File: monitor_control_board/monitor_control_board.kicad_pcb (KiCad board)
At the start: 2 copper layers, 50 x 58 mm, 21 parts, among them J2 Conn_01x08_Male, J3 Conn_01x08_Male, J5 Conn_01x05_Male, J6 Conn_01x05_Male, SW1 SW_Push, SW2 SW_Push, SW3 SW_Push, SW4 SW_Push, SW5 SW_Push, SW6 SW_Push, U1 TSSP58038

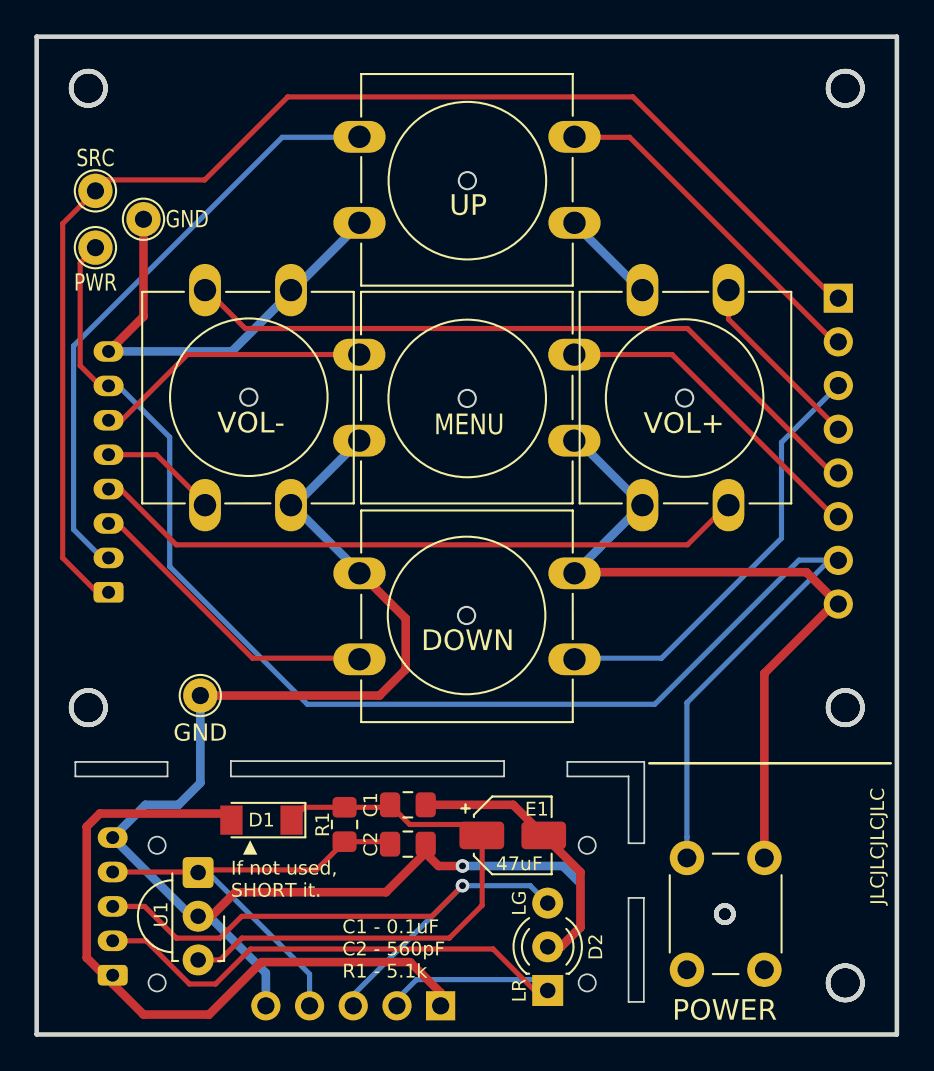
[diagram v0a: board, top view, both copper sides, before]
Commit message: 배선 및 레이아웃 최적화
Signed-off-by: Ju, Gyeong-min <jcmh74@gmail.com>
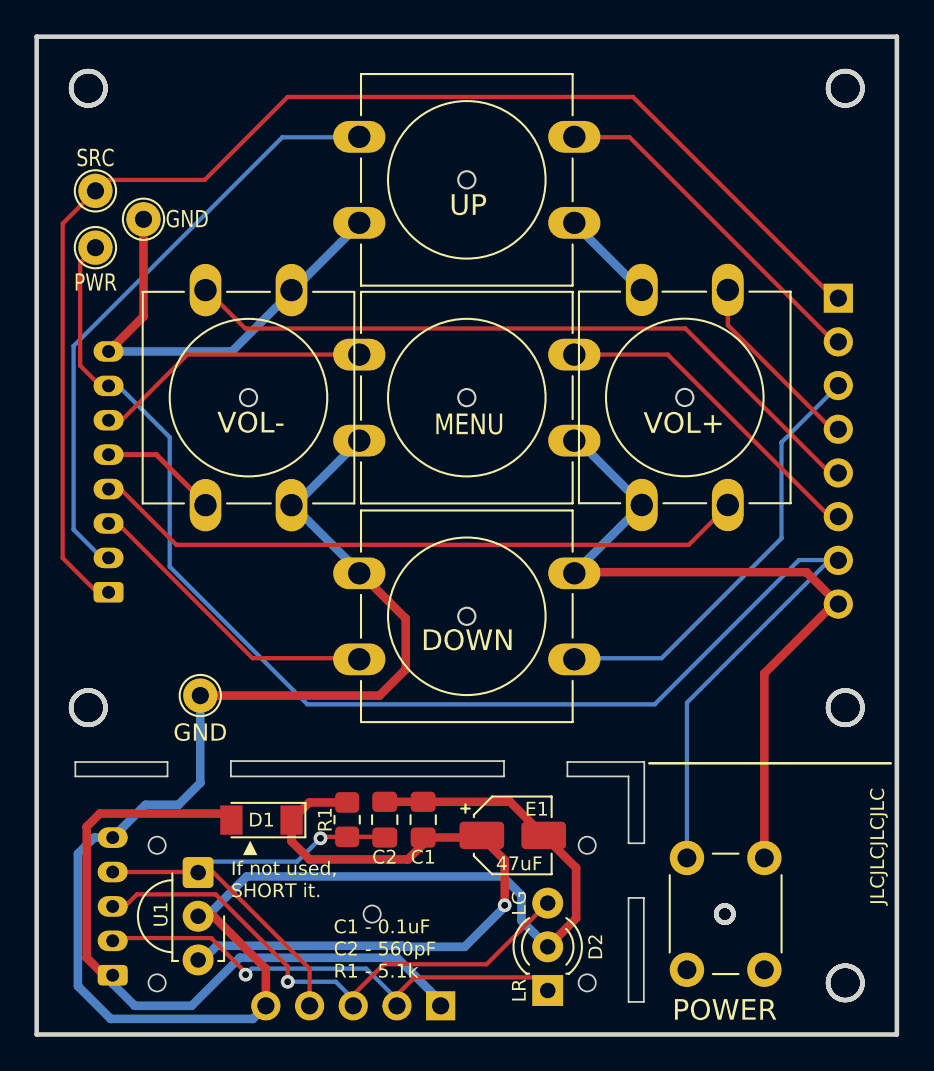
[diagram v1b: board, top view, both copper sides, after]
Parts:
- moved C2 1.96 mm to (148.9, 107.3), turned to 90 degrees
- moved C1 1.24 mm to (151.1, 107.3), turned to 90 degrees
- moved R1 0.32 mm to (146.7, 107.3)
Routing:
- net GND: track 178.4 -> 188.9 mm, vias 1 -> 0
- net /LED_R: track 38.0 -> 28.9 mm, vias 0 -> 1
- net Net-(C1-Pad1): track 34.0 -> 41.0 mm, vias 0 -> 1
- net /LED_G: track 37.3 -> 31.8 mm
- net +5V: track 41.5 -> 41.0 mm
- net /IRIN: vias 0 -> 1
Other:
- outline, holes or cut-outs redrawn

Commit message: osd 컨트롤 보드 GND 핀 추가
Signed-off-by: Ju, Gyeong-min <jcmh74@gmail.com>
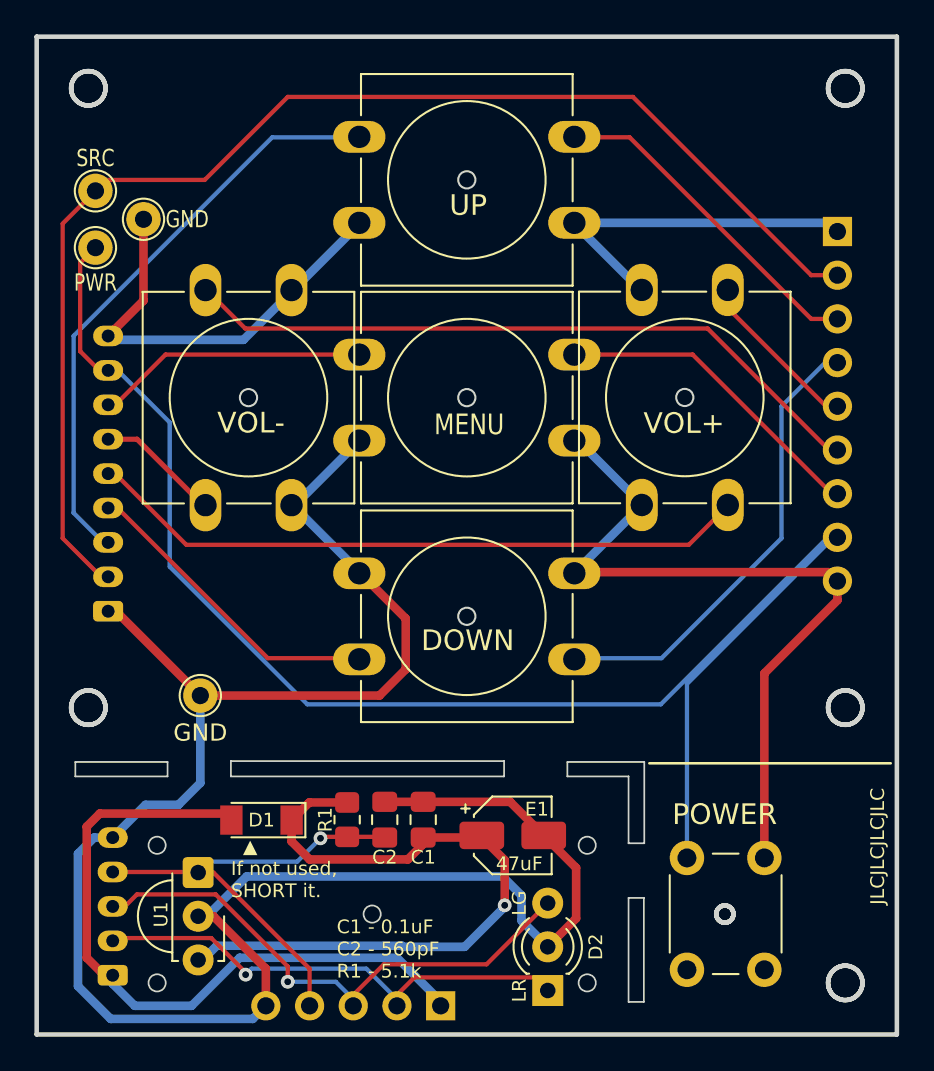
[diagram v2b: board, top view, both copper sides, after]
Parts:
- J2: value Conn_01x08_Male -> Conn_01x09_Male; footprint Connector_PinHeader_2.54mm:PinHeader_1x08_P2.54mm_Vertical -> Connector_PinHeader_2.54mm:PinHeader_1x09_P2.54mm_Vertical
- J3: value Conn_01x08_Male -> Conn_01x09_Male; footprint Connector_JST:JST_PH_S8B-PH-K_1x08_P2.00mm_Horizontal -> Connector_JST:JST_PH_S9B-PH-K_1x09_P2.00mm_Horizontal
- moved J2 3.88 mm to (175.2, 73.1)
- moved J3 1.10 mm to (132.8, 95.2)
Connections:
- J2 pad 1: /SOURCE -> GND
- J2 pad 2: /UP -> /SOURCE
- J2 pad 3: /DOWN -> /UP
- J2 pad 4: /VOL_P -> /DOWN
- J2 pad 5: /VOL_M -> /VOL_P
- J2 pad 6: /MENU -> /VOL_M
- J2 pad 7: /POWER -> /MENU
- J2 pad 8: GND -> /POWER
- J3 pad 1: /SOURCE -> GND
- J3 pad 2: /UP -> /SOURCE
- J3 pad 3: /DOWN -> /UP
- J3 pad 4: /VOL_P -> /DOWN
- J3 pad 5: /VOL_M -> /VOL_P
- J3 pad 6: /MENU -> /VOL_M
- J3 pad 7: /POWER -> /MENU
- J3 pad 8: GND -> /POWER
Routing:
- net GND: track 188.9 -> 211.3 mm
- net /DOWN: track 43.1 -> 45.2 mm
- net /POWER: track 88.5 -> 90.2 mm
- net /SOURCE: track 75.6 -> 74.2 mm
- net /UP: track 55.0 -> 54.1 mm
- net /MENU: track 35.4 -> 34.5 mm
- net /VOL_P: track 49.3 -> 48.5 mm

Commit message: 미세 조정
Signed-off-by: Ju, Gyeong-min <jcmh74@gmail.com>
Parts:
- renumbered J3 to J1, J6 to J3, J5 to J4, TP3 to TP1, TP1 to TP2, TP2 to TP3
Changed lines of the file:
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@@
   )
   (paper "A4")
+  (title_block
+    (title "Monitor OSD Control Board")
+    (date "2023-01-21")
+    (rev "4")
+    (company "Amos Home")
+  )
   (layers
     (0 "F.Cu" signal)
@@
     (property "Sheetname" "")
     (attr exclude_from_pos_files)
-    (fp_text reference "TP1" (at 0 -1.998) (layer "F.SilkS") hide
+    (fp_text reference "TP2" (at 0 -1.998) (layer "F.SilkS") hide
       (effects (font (size 1 1) (thickness 0.15)))
     )
@@
     (property "Sheetname" "")
     (attr exclude_from_pos_files)
-    (fp_text reference "TP3" (at 0 -1.998) (layer "F.SilkS") hide
+    (fp_text reference "TP1" (at 0 -1.998) (layer "F.SilkS") hide
       (effects (font (size 1 1) (thickness 0.15)))
     )
@@
     (property "Sheetname" "")
     (attr exclude_from_pos_files)
-    (fp_text reference "TP2" (at 0 -1.998) (layer "F.SilkS") hide
+    (fp_text reference "TP3" (at 0 -1.998) (layer "F.SilkS") hide
       (effects (font (size 1 1) (thickness 0.15)))
     )
@@
     (property "Sheetname" "")
     (attr through_hole)
-    (fp_text reference "J5" (at 0 2.032 90) (layer "B.SilkS")
+    (fp_text reference "J4" (at 0 2.0828 180) (layer "B.SilkS")
       (effects (font (size 0.8 0.8) (thickness 0.15)) (justify mirror))
     )
@@
     (property "Sheetname" "")
     (attr through_hole)
-    (fp_text reference "J3" (at 8 -2.45 270) (layer "B.SilkS")
-      (effects (font (size 1 1) (thickness 0.15)) (justify mirror))
+    (fp_text reference "J1" (at 8 -2.5654 270) (layer "B.SilkS")
+      (effects (font (size 0.8 0.8) (thickness 0.15)) (justify mirror))
     )
     (fp_text value "Conn_01x09_Male" (at 8 -7.45 270) (layer "B.Fab")
@@
     (property "Sheetname" "")
     (attr through_hole)
-    (fp_text reference "J2" (at 0 2.33) (layer "B.SilkS")
-      (effects (font (size 1 1) (thickness 0.15)) (justify mirror))
+    (fp_text reference "J2" (at 0 2.33 90) (layer "B.SilkS")
+      (effects (font (size 0.8 0.8) (thickness 0.15)) (justify mirror))
     )
     (fp_text value "Conn_01x09_Male" (at 0 -22.65) (layer "B.Fab")
@@
     (property "Sheetname" "")
     (attr through_hole)
-    (fp_text reference "J6" (at 4.318 -3.2882 90) (layer "B.SilkS")
+    (fp_text reference "J3" (at 4.0132 -2.577 90) (layer "B.SilkS")
       (effects (font (size 0.8 0.8) (thickness 0.15)) (justify mirror))
     )

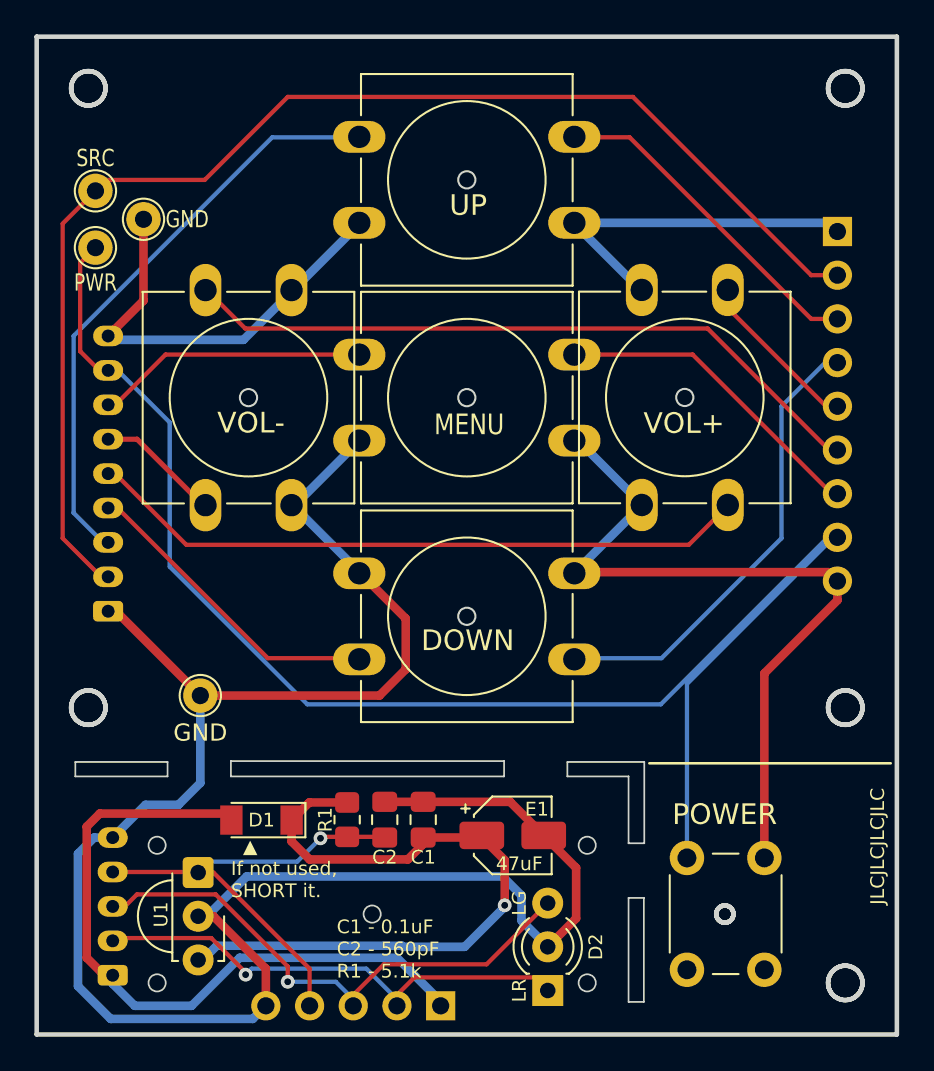
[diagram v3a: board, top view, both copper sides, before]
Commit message: monitor_osd_board 마킹 및 리소스 추가
Signed-off-by: Ju, Gyeong-min <jcmh74@gmail.com>
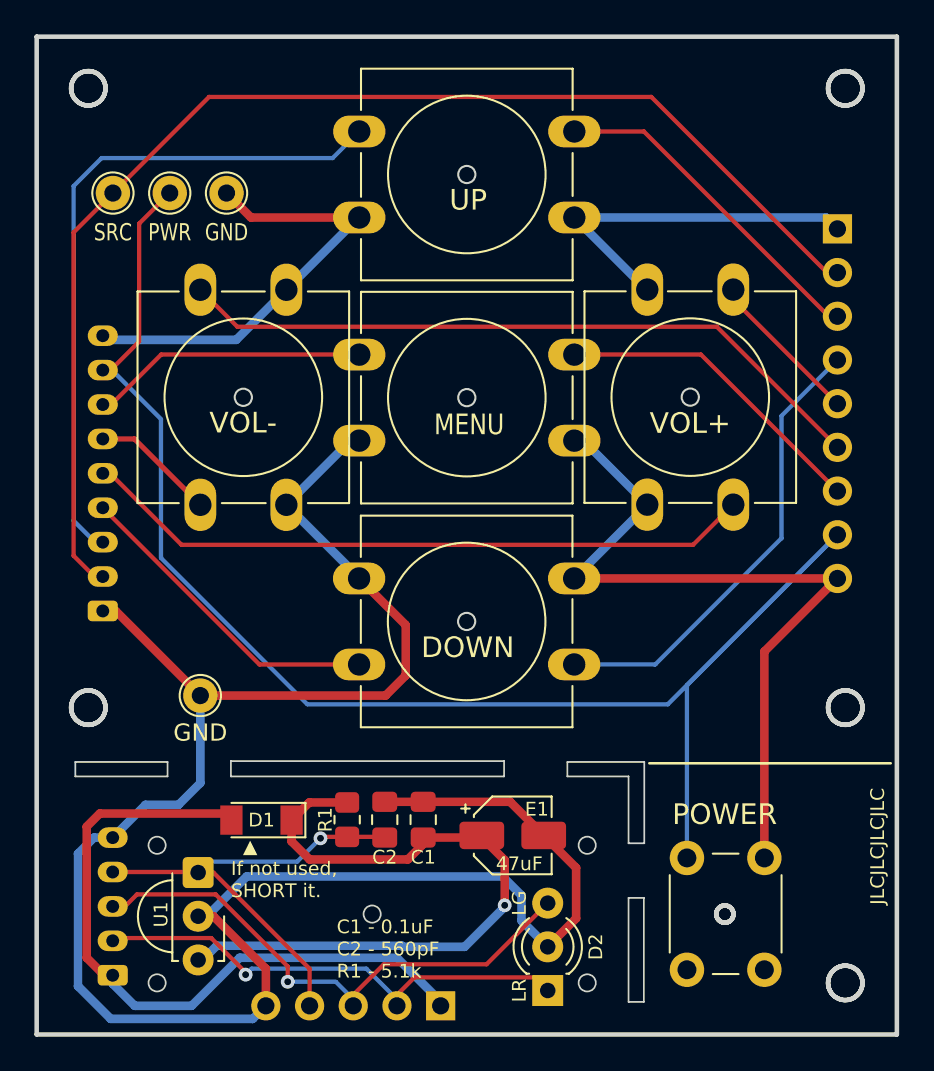
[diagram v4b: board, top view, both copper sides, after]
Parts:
- moved TP1 5.36 mm to (136.4, 70.9)
- moved TP3 5.06 mm to (139.7, 70.9)
- moved TP2 1.02 mm to (133.1, 70.9)
- moved SW5 0.32 mm to (169.2, 76.5)
- moved J1 0.31 mm to (132.5, 95.2)
- moved SW2 0.31 mm to (147.4, 67.3)
- moved SW1 0.30 mm to (138.2, 89.0)
- moved SW4 0.30 mm to (159.9, 98.3)
- moved J2 0.15 mm to (175.2, 72.9)
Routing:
- net /UP: track 54.1 -> 59.3 mm
- net /POWER: track 90.2 -> 94.1 mm
- net GND: track 211.3 -> 214.5 mm
- net /SOURCE: track 74.2 -> 72.9 mm

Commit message: monitor_osd 배선 최적화
Signed-off-by: Ju, Gyeong-min <jcmh74@gmail.com>
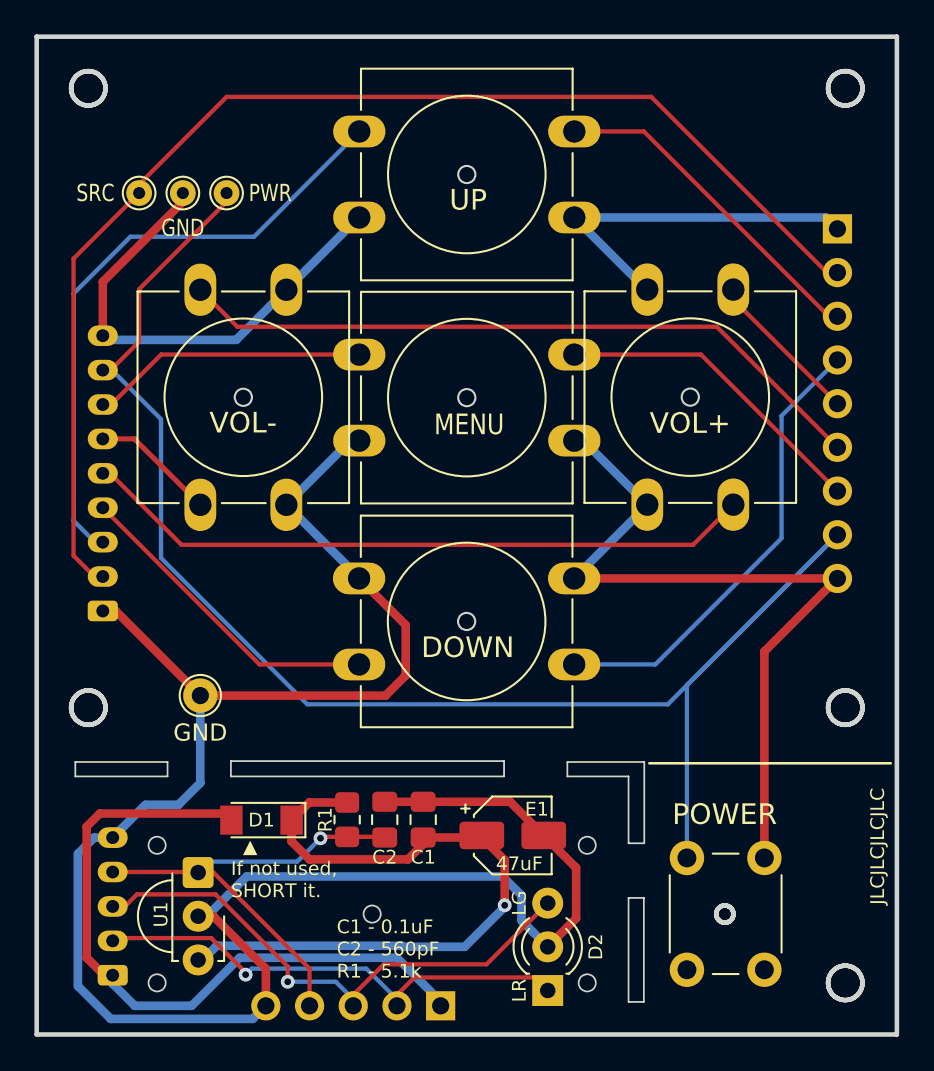
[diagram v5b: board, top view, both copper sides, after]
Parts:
- TP1, TP2, TP3: footprint TestPoint:TestPoint_THTPad_D2.0mm_Drill1.0mm -> TestPoint:TestPoint_THTPad_D1.5mm_Drill0.7mm
- moved TP1 3.30 mm to (139.7, 70.9)
- moved TP3 2.54 mm to (137.2, 70.9)
- moved TP2 1.52 mm to (134.6, 70.9)
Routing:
- net /UP: track 59.3 -> 55.7 mm
- net GND: track 214.5 -> 216.4 mm
- net /POWER: track 94.1 -> 95.5 mm
- net /SOURCE: track 72.9 -> 72.3 mm

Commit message: osd_control 보드 마우스 바이트 추가
Signed-off-by: Ju, Gyeong-min <jcmh74@gmail.com>
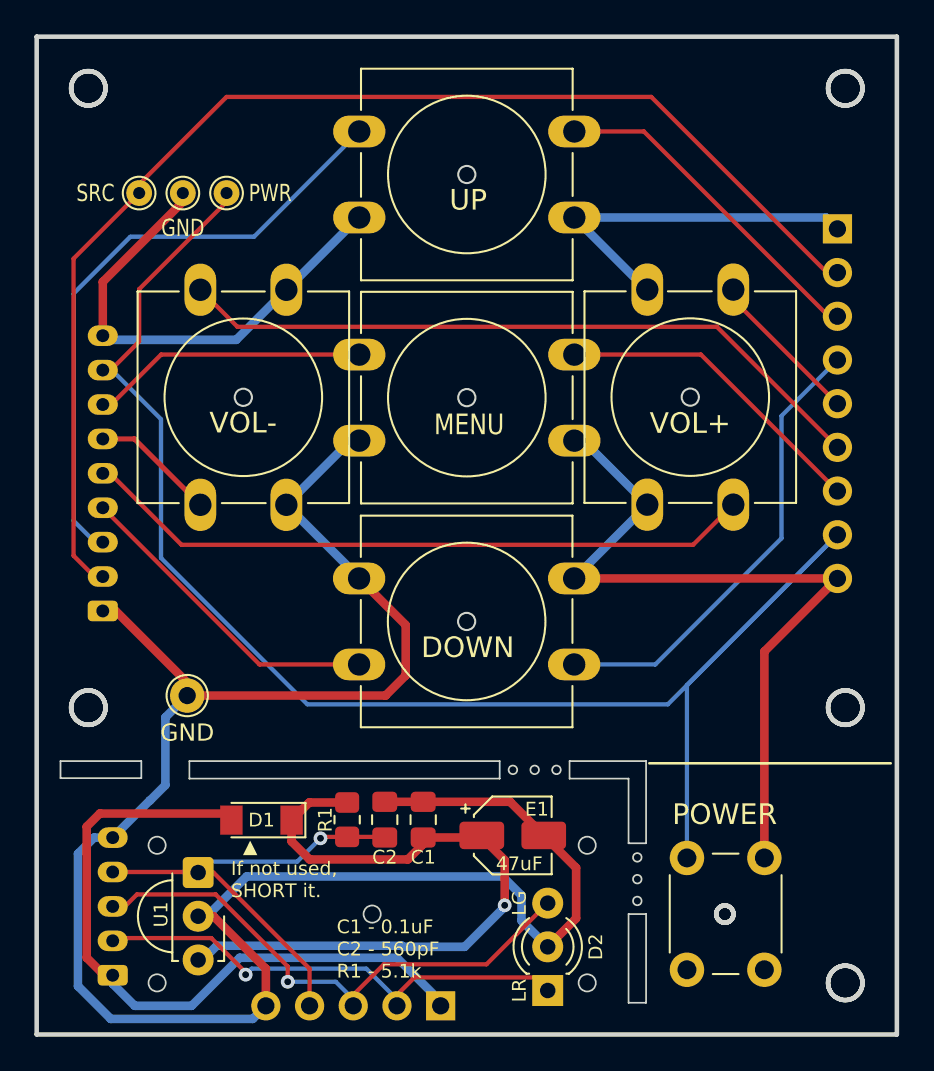
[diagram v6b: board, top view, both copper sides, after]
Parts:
- moved TP4 0.76 mm to (137.4, 100.1)
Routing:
- net GND: track 216.4 -> 215.4 mm
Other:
- outline, holes or cut-outs redrawn
- board text removed: "JLCJLCJLCJLC"
